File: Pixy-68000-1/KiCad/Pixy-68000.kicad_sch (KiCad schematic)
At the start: 93 parts, among them J1 AVR_ISP, J11 SPI, J11 USB, J12 CPUSIGNAL, J4 Socket5, J5 Socket5, J6 JTAG, J6 Socket5, J7 Socket5, J8 BUS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

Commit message: Added memory selector headers.
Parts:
- added J10: MEMSIGNAL, kekyo:PinSocket_1x05_P2.54mm_Vertical, symbol kekyo:Socket5
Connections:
- net GND: now also J10.5 (P4)
- net /PROMCS0: now also J10.1 (P0)
- net /PROMCS1: now also J10.2 (P1)
- net /SRAMCS0: now also J10.3 (P2)
- net /SRAMCS1: now also J10.4 (P3)
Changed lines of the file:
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@@
     (stroke (width 0) (type default))
   )
+  (bus_entry (at 496.57 317.5) (size 2.54 2.54)
+    (stroke (width 0) (type default))
+  )
   (bus_entry (at 496.57 219.71) (size 2.54 2.54)
     (stroke (width 0) (type default))
@@
     (stroke (width 0) (type default))
   )
+  (bus_entry (at 496.57 320.04) (size 2.54 2.54)
+    (stroke (width 0) (type default))
+  )
   (bus_entry (at 135.89 196.85) (size 2.54 -2.54)
     (stroke (width 0) (type default))
@@
     (stroke (width 0) (type default))
   )
+  (bus_entry (at 496.57 312.42) (size 2.54 2.54)
+    (stroke (width 0) (type default))
+  )
   (bus_entry (at 60.96 170.18) (size 2.54 2.54)
     (stroke (width 0) (type default))
@@
     (stroke (width 0) (type default))
   )
+  (bus_entry (at 496.57 314.96) (size 2.54 2.54)
+    (stroke (width 0) (type default))
+  )
   (bus_entry (at 388.62 106.68) (size -2.54 2.54)
     (stroke (width 0) (type default))
@@
     (stroke (width 0) (type default))
   )
+  (bus (pts (xy 496.57 317.5) (xy 496.57 320.04))
+    (stroke (width 0) (type default))
+  )
   (wire (pts (xy 391.16 137.16) (xy 402.59 137.16))
     (stroke (width 0) (type default))
@@
     (stroke (width 0) (type default))
   )
+  (wire (pts (xy 499.11 314.96) (xy 515.62 314.96))
+    (stroke (width 0) (type default))
+  )
   (wire (pts (xy 87.63 377.19) (xy 100.33 377.19))
     (stroke (width 0) (type default))
@@
     (stroke (width 0) (type default))
   )
+  (bus (pts (xy 496.57 312.42) (xy 496.57 314.96))
+    (stroke (width 0) (type default))
+  )
   (wire (pts (xy 43.18 379.73) (xy 43.18 375.92))
     (stroke (width 0) (type default))
@@
     (stroke (width 0) (type default))
   )
+  (wire (pts (xy 511.81 325.12) (xy 511.81 334.01))
+    (stroke (width 0) (type default))
+  )
   (bus (pts (xy 297.18 312.42) (xy 297.18 314.96))
     (stroke (width 0) (type default))
@@
     (stroke (width 0) (type default))
   )
+  (wire (pts (xy 511.81 325.12) (xy 515.62 325.12))
+    (stroke (width 0) (type default))
+  )
   (wire (pts (xy 121.92 294.64) (xy 121.92 302.26))
     (stroke (width 0) (type default))
@@
     (stroke (width 0) (type default))
   )
+  (wire (pts (xy 499.11 320.04) (xy 515.62 320.04))
+    (stroke (width 0) (type default))
+  )
   (wire (pts (xy 242.57 392.43) (xy 252.73 392.43))
     (stroke (width 0) (type default))
@@
     (stroke (width 0) (type default))
   )
+  (wire (pts (xy 499.11 322.58) (xy 515.62 322.58))
+    (stroke (width 0) (type default))
+  )
   (bus (pts (xy 496.57 245.11) (xy 496.57 247.65))
     (stroke (width 0) (type default))
@@
     (stroke (width 0) (type default))
   )
+  (wire (pts (xy 499.11 317.5) (xy 515.62 317.5))
+    (stroke (width 0) (type default))
+  )
   (wire (pts (xy 63.5 167.64) (xy 74.93 167.64))
     (stroke (width 0) (type default))
@@
     (stroke (width 0) (type default))
   )
+  (bus (pts (xy 496.57 314.96) (xy 496.57 317.5))
+    (stroke (width 0) (type default))
+  )
   (wire (pts (xy 204.47 292.1) (xy 204.47 223.52))
     (stroke (width 0) (type default))
@@
     (stroke (width 0) (type default))
   )
+  (bus (pts (xy 496.57 293.37) (xy 496.57 312.42))
+    (stroke (width 0) (type default))
+  )
   (wire (pts (xy 184.15 177.8) (xy 210.82 177.8))
     (stroke (width 0) (type default))
@@
     (effects (font (size 1.27 1.27)) (justify left bottom))
   )
+  (label "{slash}SRAMCS0" (at 499.11 320.04 0) (fields_autoplaced)
+    (effects (font (size 1.27 1.27)) (justify left bottom))
+  )
   (label "A3" (at 391.16 114.3 0) (fields_autoplaced)
     (effects (font (size 1.27 1.27)) (justify left bottom))
@@
     (effects (font (size 1.27 1.27)) (justify left bottom))
   )
+  (label "{slash}PROMCS1" (at 499.11 317.5 0) (fields_autoplaced)
+    (effects (font (size 1.27 1.27)) (justify left bottom))
+  )
   (label "D3" (at 491.49 119.38 0) (fields_autoplaced)
     (effects (font (size 1.27 1.27)) (justify left bottom))
@@
     (effects (font (size 1.27 1.27)) (justify left bottom))
   )
+  (label "{slash}SRAMCS1" (at 499.11 322.58 0) (fields_autoplaced)
+    (effects (font (size 1.27 1.27)) (justify left bottom))
+  )
   (label "{slash}PROMCS0" (at 184.15 182.88 0) (fields_autoplaced)
     (effects (font (size 1.27 1.27)) (justify left bottom))
@@
     (effects (font (size 1.27 1.27)) (justify left bottom))
   )
+  (label "{slash}PROMCS0" (at 499.11 314.96 0) (fields_autoplaced)
+    (effects (font (size 1.27 1.27)) (justify left bottom))
+  )
   (label "{slash}RESET" (at 130.81 93.98 90) (fields_autoplaced)
     (effects (font (size 1.27 1.27)) (justify left bottom))
@@
     )
   )
+  (symbol (lib_id "kekyo:Socket5") (at 527.05 320.04 0) (mirror y) (unit 1)
+    (in_bom yes) (on_board yes) (dnp no)
+    (property "Reference" "J10" (at 530.86 317.5 0)
+      (effects (font (size 1.27 1.27)))
+    )
+    (property "Value" "MEMSIGNAL" (at 533.4 320.04 0)
+      (effects (font (size 1.27 1.27)))
+    )
+    (property "Footprint" "kekyo:PinSocket_1x05_P2.54mm_Vertical" (at 523.24 331.47 0)
+      (effects (font (size 1.27 1.27)) hide)
+    )
+    (property "Datasheet" "~" (at 524.51 334.01 0)
+      (effects (font (size 1.27 1.27)) hide)
+    )
+    (pin "1")
+    (pin "2")
+    (pin "3")
+    (pin "4")
+    (pin "5")
+    (instances
+      (project "Pixy-68000"
+        (path "/9aeb2b9d-08f7-44b5-9289-68c429469433"
+          (reference "J10") (unit 1)
+        )
+      )
+    )
+  )
   (symbol (lib_name "C_3") (lib_id "kekyo:C") (at 130.81 384.81 0) (unit 1)
     (in_bom yes) (on_board yes) (dnp no) (fields_autoplaced)
@@
         )
       )
+    )
+  )
+  (symbol (lib_id "power:GND") (at 511.81 334.01 0) (unit 1)
+    (in_bom yes) (on_board yes) (dnp no) (fields_autoplaced)
+    (property "Reference" "#PWR02" (at 511.81 340.36 0)
+      (effects (font (size 1.27 1.27)) hide)
+    )
+    (property "Value" "GND" (at 511.81 339.09 0)
+      (effects (font (size 1.27 1.27)))
+    )
+    (property "Footprint" "" (at 511.81 334.01 0)
+      (effects (font (size 1.27 1.27)) hide)
+    )
+    (property "Datasheet" "" (at 511.81 334.01 0)
+      (effects (font (size 1.27 1.27)) hide)
+    )
+    (pin "1")
+    (instances
+      (project "MC68SEC000"
+        (path "/7907391b-035a-42ea-89b1-82b781ee98c8"
+          (reference "#PWR02") (unit 1)
+        )
+      )
+      (project "Pixy-68000"
+        (path "/9aeb2b9d-08f7-44b5-9289-68c429469433"
+          (reference "#PWR042") (unit 1)
+        )
+      )

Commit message: Fixed exchanged RAM/PROM selector.
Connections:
- net /PROMCS0: now also R14.2, U11.22 (CE), U4.29 (PB4C); no longer R15.2, U10.22 (CE), U4.30 (PB4D)
- net /PROMCS1: now also R15.2, U10.22 (CE), U4.30 (PB4D); no longer R14.2, U11.22 (CE), U4.29 (PB4C)
- net /SRAMCS0: now also R14.2, U4.27 (PB4A/CSSPIN), U7.8 (~{CE}); no longer R15.2, U4.28 (PB4B), U6.8 (~{CE})
- net /SRAMCS1: now also R15.2, U4.28 (PB4B), U6.8 (~{CE}); no longer R14.2, U4.27 (PB4A/CSSPIN), U7.8 (~{CE})
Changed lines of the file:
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@@
+    (effects (font (size 1.27 1.27)) (justify left bottom))
+  )
+  (label "{slash}PROMCS1" (at 184.15 182.88 0) (fields_autoplaced)
     (effects (font (size 1.27 1.27)) (justify left bottom))
   )
@@
     (effects (font (size 1.27 1.27)) (justify left bottom))
   )
-  (label "{slash}SRAMCS1" (at 391.16 160.02 0) (fields_autoplaced)
-    (effects (font (size 1.27 1.27)) (justify left bottom))
-  )
   (label "{slash}RESETAVR" (at 124.46 294.64 0) (fields_autoplaced)
     (effects (font (size 1.27 1.27)) (justify left bottom))
@@
     (effects (font (size 1.27 1.27)) (justify left bottom))
   )
+  (label "{slash}SRAMCS0" (at 391.16 160.02 0) (fields_autoplaced)
+    (effects (font (size 1.27 1.27)) (justify left bottom))
+  )
   (label "D7" (at 499.11 227.33 0) (fields_autoplaced)
     (effects (font (size 1.27 1.27)) (justify left bottom))
@@
     (effects (font (size 1.27 1.27)) (justify left bottom))
   )
-  (label "{slash}PROMCS1" (at 499.11 167.64 0) (fields_autoplaced)
-    (effects (font (size 1.27 1.27)) (justify left bottom))
-  )
   (label "A15" (at 132.08 161.29 0) (fields_autoplaced)
     (effects (font (size 1.27 1.27)) (justify left bottom))
@@
     (effects (font (size 1.27 1.27)) (justify left bottom))
   )
+  (label "{slash}PROMCS1" (at 367.03 93.98 90) (fields_autoplaced)
+    (effects (font (size 1.27 1.27)) (justify left bottom))
+  )
   (label "D13" (at 433.07 121.92 0) (fields_autoplaced)
     (effects (font (size 1.27 1.27)) (justify left bottom))
@@
     (effects (font (size 1.27 1.27)) (justify left bottom))
   )
+  (label "{slash}PROMCS0" (at 184.15 180.34 0) (fields_autoplaced)
+    (effects (font (size 1.27 1.27)) (justify left bottom))
+  )
   (label "FC0" (at 63.5 152.4 0) (fields_autoplaced)
     (effects (font (size 1.27 1.27)) (justify left bottom))
@@
     (effects (font (size 1.27 1.27)) (justify left bottom))
   )
+  (label "{slash}SRAMCS0" (at 184.15 175.26 0) (fields_autoplaced)
+    (effects (font (size 1.27 1.27)) (justify left bottom))
+  )
   (label "{slash}BG" (at 499.11 295.91 0) (fields_autoplaced)
     (effects (font (size 1.27 1.27)) (justify left bottom))
   )
-  (label "{slash}PROMCS1" (at 360.68 93.98 90) (fields_autoplaced)
-    (effects (font (size 1.27 1.27)) (justify left bottom))
-  )
   (label "A13" (at 441.96 142.24 0) (fields_autoplaced)
     (effects (font (size 1.27 1.27)) (justify left bottom))
@@
     (effects (font (size 1.27 1.27)) (justify left bottom))
   )
-  (label "{slash}PROMCS0" (at 184.15 182.88 0) (fields_autoplaced)
-    (effects (font (size 1.27 1.27)) (justify left bottom))
-  )
   (label "A7" (at 184.15 215.9 0) (fields_autoplaced)
     (effects (font (size 1.27 1.27)) (justify left bottom))
@@
     (effects (font (size 1.27 1.27)) (justify left bottom))
   )
-  (label "{slash}PROMCS0" (at 441.96 167.64 0) (fields_autoplaced)
-    (effects (font (size 1.27 1.27)) (justify left bottom))
-  )
   (label "{slash}STEPEN" (at 68.58 93.98 90) (fields_autoplaced)
     (effects (font (size 1.27 1.27)) (justify left bottom))
@@
     (effects (font (size 1.27 1.27)) (justify left bottom))
   )
-  (label "{slash}SRAMCS1" (at 347.98 93.98 90) (fields_autoplaced)
-    (effects (font (size 1.27 1.27)) (justify left bottom))
-  )
   (label "MCLK" (at 335.28 93.98 90) (fields_autoplaced)
     (effects (font (size 1.27 1.27)) (justify left bottom))
@@
     (effects (font (size 1.27 1.27)) (justify left bottom))
   )
+  (label "{slash}SRAMCS0" (at 347.98 93.98 90) (fields_autoplaced)
+    (effects (font (size 1.27 1.27)) (justify left bottom))
+  )
   (label "PROGRAMN" (at 210.82 345.44 0) (fields_autoplaced)
     (effects (font (size 1.27 1.27)) (justify left bottom))
@@
     (effects (font (size 1.27 1.27)) (justify left bottom))
   )
-  (label "{slash}PROMCS1" (at 184.15 180.34 0) (fields_autoplaced)
-    (effects (font (size 1.27 1.27)) (justify left bottom))
-  )
   (label "A22" (at 303.53 208.28 0) (fields_autoplaced)
     (effects (font (size 1.27 1.27)) (justify left bottom))
@@
     (effects (font (size 1.27 1.27)) (justify left bottom))
   )
+  (label "{slash}PROMCS0" (at 499.11 167.64 0) (fields_autoplaced)
+    (effects (font (size 1.27 1.27)) (justify left bottom))
+  )
   (label "{slash}HALT" (at 184.15 144.78 0) (fields_autoplaced)
     (effects (font (size 1.27 1.27)) (justify left bottom))
@@
     (effects (font (size 1.27 1.27)) (justify left bottom))
   )
+  (label "{slash}PROMCS0" (at 360.68 93.98 90) (fields_autoplaced)
+    (effects (font (size 1.27 1.27)) (justify left bottom))
+  )
   (label "{slash}SW2" (at 210.82 312.42 0) (fields_autoplaced)
     (effects (font (size 1.27 1.27)) (justify left bottom))
@@
     (effects (font (size 1.27 1.27)) (justify left bottom))
   )
-  (label "{slash}SRAMCS0" (at 354.33 93.98 90) (fields_autoplaced)
+  (label "{slash}PROMCS1" (at 441.96 167.64 0) (fields_autoplaced)
     (effects (font (size 1.27 1.27)) (justify left bottom))
   )
@@
     (effects (font (size 1.27 1.27)) (justify left bottom))
   )
-  (label "{slash}PROMCS0" (at 367.03 93.98 90) (fields_autoplaced)
-    (effects (font (size 1.27 1.27)) (justify left bottom))
-  )
   (label "A2" (at 499.11 114.3 0) (fields_autoplaced)
     (effects (font (size 1.27 1.27)) (justify left bottom))
@@
     (effects (font (size 1.27 1.27)) (justify left bottom))
   )
-  (label "{slash}SRAMCS0" (at 340.36 160.02 0) (fields_autoplaced)
-    (effects (font (size 1.27 1.27)) (justify left bottom))
-  )
   (label "A13" (at 391.16 139.7 0) (fields_autoplaced)
     (effects (font (size 1.27 1.27)) (justify left bottom))
@@
     (effects (font (size 1.27 1.27)) (justify left bottom))
   )
+  (label "{slash}SRAMCS1" (at 184.15 177.8 0) (fields_autoplaced)
+    (effects (font (size 1.27 1.27)) (justify left bottom))
+  )
   (label "A10" (at 132.08 148.59 0) (fields_autoplaced)
     (effects (font (size 1.27 1.27)) (justify left bottom))
@@
     (effects (font (size 1.27 1.27)) (justify left bottom))
   )
+  (label "{slash}SRAMCS1" (at 354.33 93.98 90) (fields_autoplaced)
+    (effects (font (size 1.27 1.27)) (justify left bottom))
+  )
   (label "D12" (at 303.53 190.5 0) (fields_autoplaced)
     (effects (font (size 1.27 1.27)) (justify left bottom))
@@
     (effects (font (size 1.27 1.27)) (justify left bottom))
   )
+  (label "{slash}SRAMCS1" (at 340.36 160.02 0) (fields_autoplaced)
+    (effects (font (size 1.27 1.27)) (justify left bottom))
+  )
   (label "REQINT" (at 210.82 342.9 0) (fields_autoplaced)
     (effects (font (size 1.27 1.27)) (justify left bottom))
@@
     (effects (font (size 1.27 1.27)) (justify left bottom))
   )
-  (label "{slash}SRAMCS0" (at 184.15 177.8 0) (fields_autoplaced)
-    (effects (font (size 1.27 1.27)) (justify left bottom))
-  )
   (label "{slash}BERR" (at 544.83 295.91 0) (fields_autoplaced)
     (effects (font (size 1.27 1.27)) (justify left bottom))
@@
     (effects (font (size 1.27 1.27)) (justify left bottom))
   )
-  (label "{slash}SRAMCS1" (at 184.15 175.26 0) (fields_autoplaced)
-    (effects (font (size 1.27 1.27)) (justify left bottom))
-  )

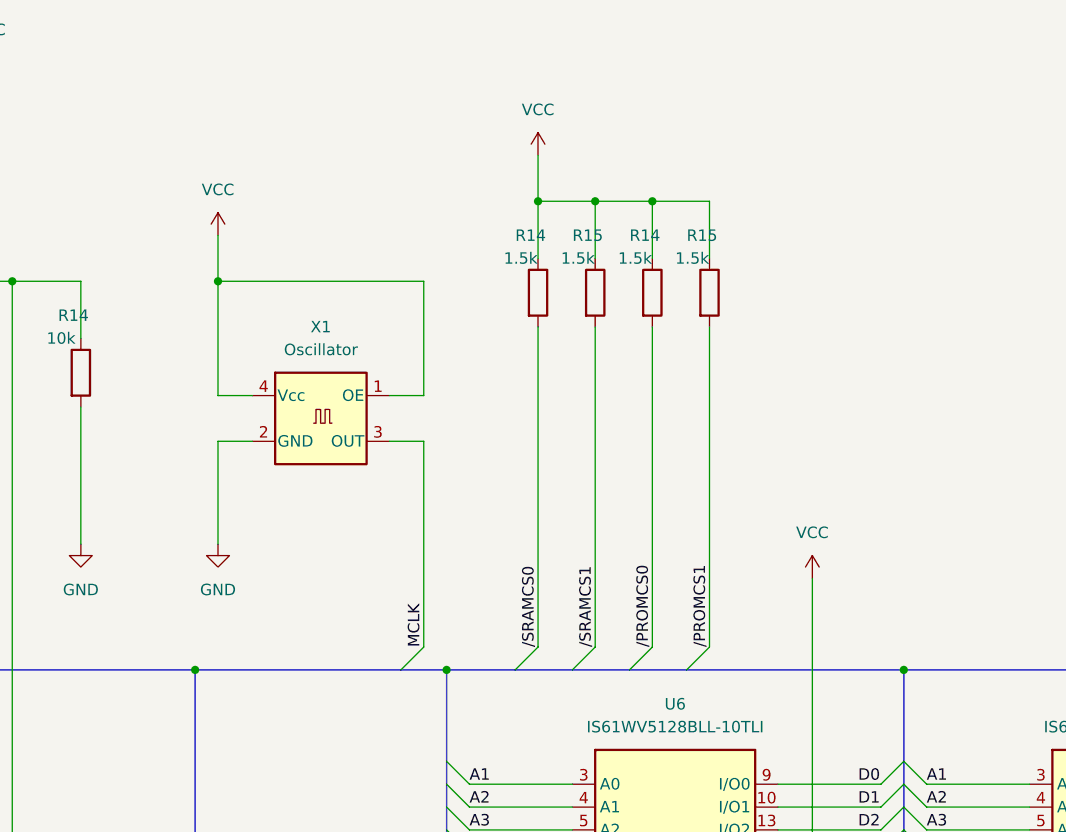
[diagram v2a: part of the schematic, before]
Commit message: Added /OE pullup register.
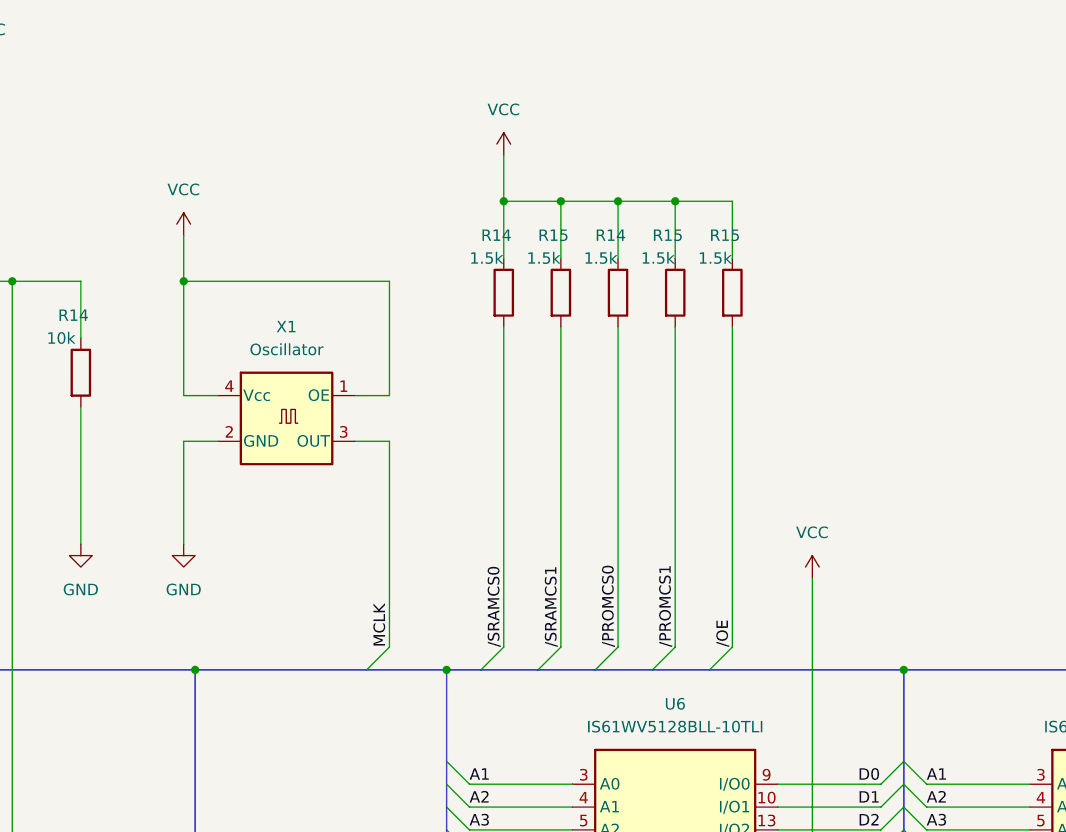
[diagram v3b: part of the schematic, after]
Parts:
- added R15: 1.5k, kekyo:R_0805_2012, symbol Device:R
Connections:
- net VCC: now also R15.1
- net /OE: now also R15.2
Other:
- moved on the sheet: R14, R15, X1
